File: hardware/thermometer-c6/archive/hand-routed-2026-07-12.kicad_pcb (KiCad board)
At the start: 2 copper layers, 49 x 36 mm, 100 parts, among them J1 JST-PH-2 BAT, J2 MEAS_HDR, J3 USB-C, J4 EPD FPC24 0.5mm, J5 DEBUG, Q1 AO3401A, Q2 AO3401A, Q3 Si1308EDL, Q4 AO3401A, Q5 2N7002, Q6 AO3401A, SW1 RESET, SW2 BOOT, U1 ESP32-C6-MINI-1-N4, U2 RT9080-33GJ5, U3 USBLC6-2SC6, U4 MCP73831-2, U5 BMP581, U6 BMP585, Y1 32.768kHz FC-135

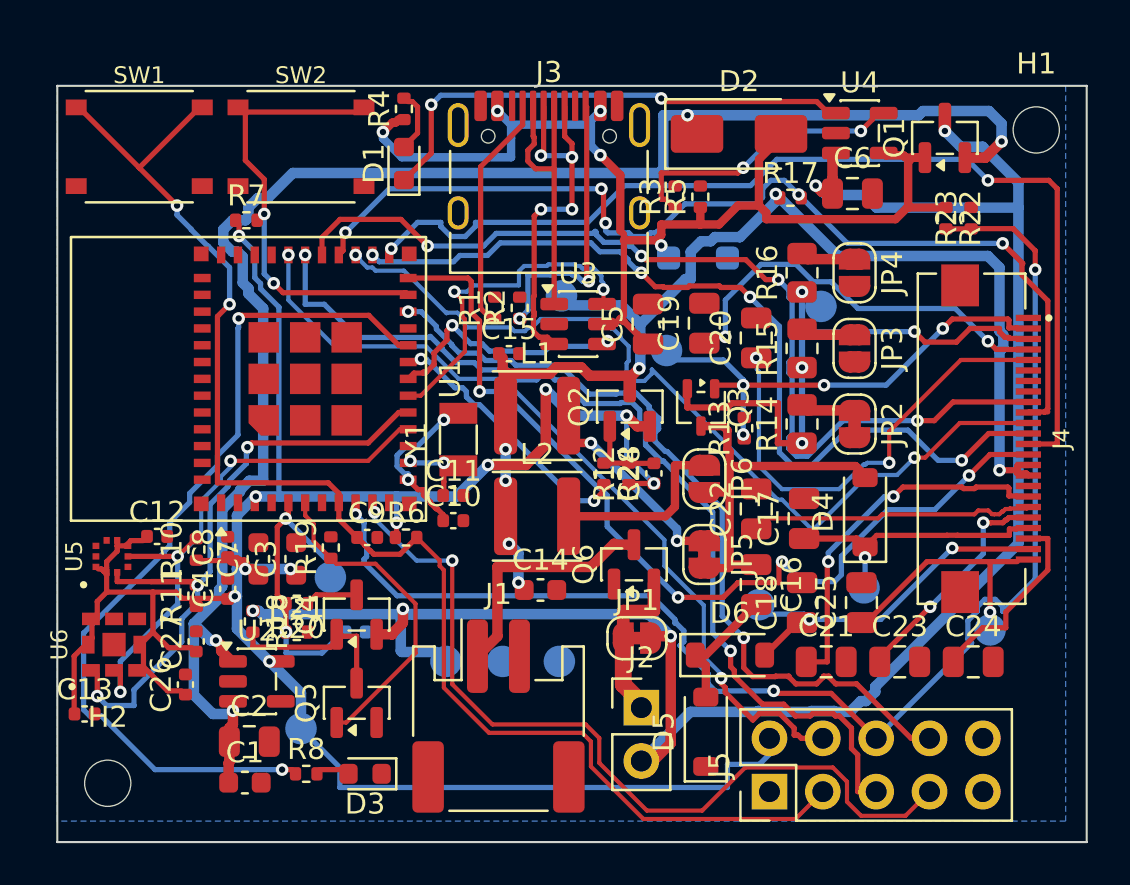
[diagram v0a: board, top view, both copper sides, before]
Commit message: Complete M5: R9 restored + GUI-routed, harvest round-trip hardened
The user routed R9's pads in the GUI (moving the +3V3 B.Cu trunk locally
to make space); re-harvested wholesale. extract_tracks.py now imports
under PCB_NO_ROUTES (a shell redirect into pcb_routes.py truncated the
module before its own transitive import -- the failure emptied the file)
and gains -o for atomic output; never use shell redirection for the
harvest. LED_STATUS's west descent gets a 0.15mm jog in the data: its
45-degree corner was exactly tangent to the antenna keep-out corner
(check_pcb intersect-fail at 0.000mm) while the SDA via east of the
descent leaves only a 7um-margin lane -- the jog threads both.

Gates: make check green, check_pcb OK, DRC zero copper violations,
unconnected = GND-only (M6 pour), byte-stable render. The archive
snapshot is refreshed to the user's final GUI save (the LED jog exists
only in pcb_routes.py).

Co-Authored-By: Claude Fable 5 <noreply@anthropic.com>
Claude-Session: https://claude.ai/code/session_017pkZ81qmZpNwwW2CABSh5y
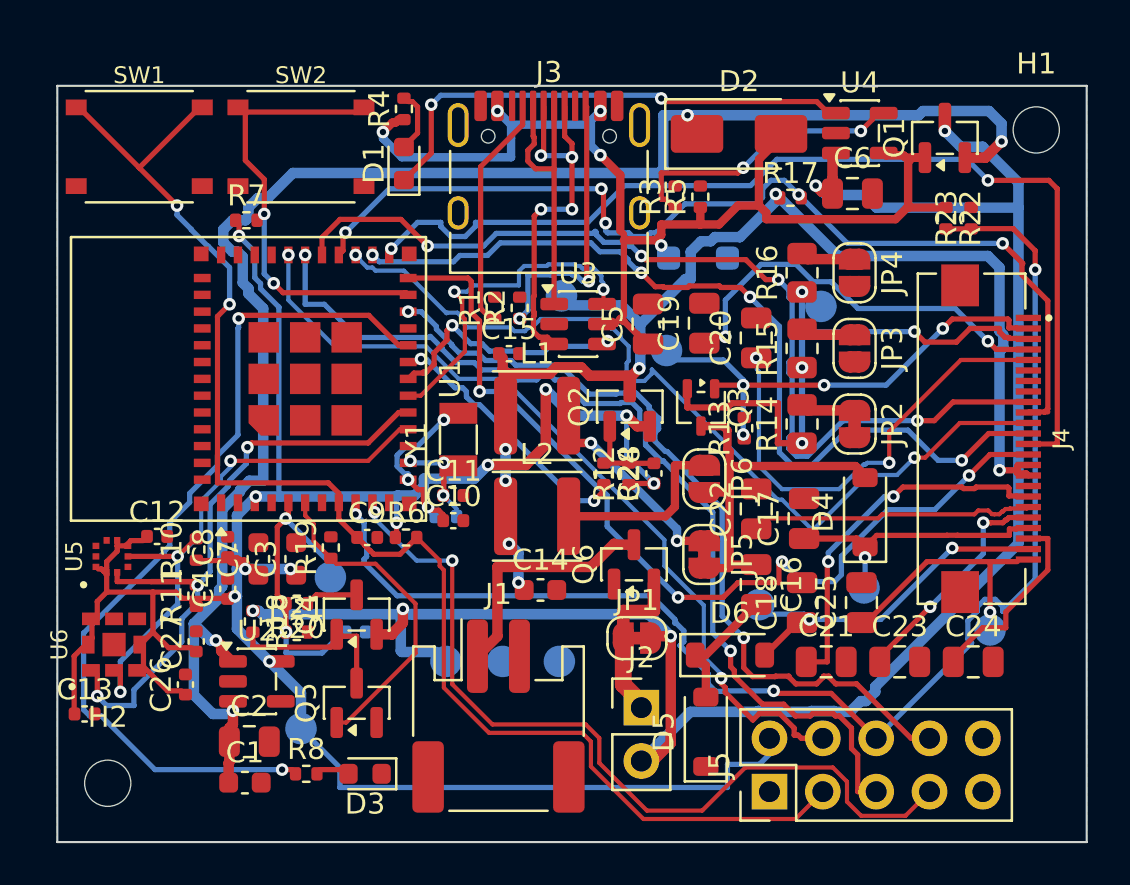
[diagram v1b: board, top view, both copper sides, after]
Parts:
- added R9: 10M, Resistor_SMD:R_0402_1005Metric, B.Cu at (118.5, 120.5)
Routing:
- net XTAL_32K_N: track 2.99 -> 4.26 mm, vias 2 -> 3
- net XTAL_32K_P: track 8.03 -> 8.80 mm, vias 2 -> 3
